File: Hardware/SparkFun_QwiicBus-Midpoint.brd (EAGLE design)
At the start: 45.7 x 27.9 mm, 69 parts, among them J1 QWIIC, J2 QWIIC, J3 RJ45, J7 RJ45, U1 PCA9615, U2 3.3V

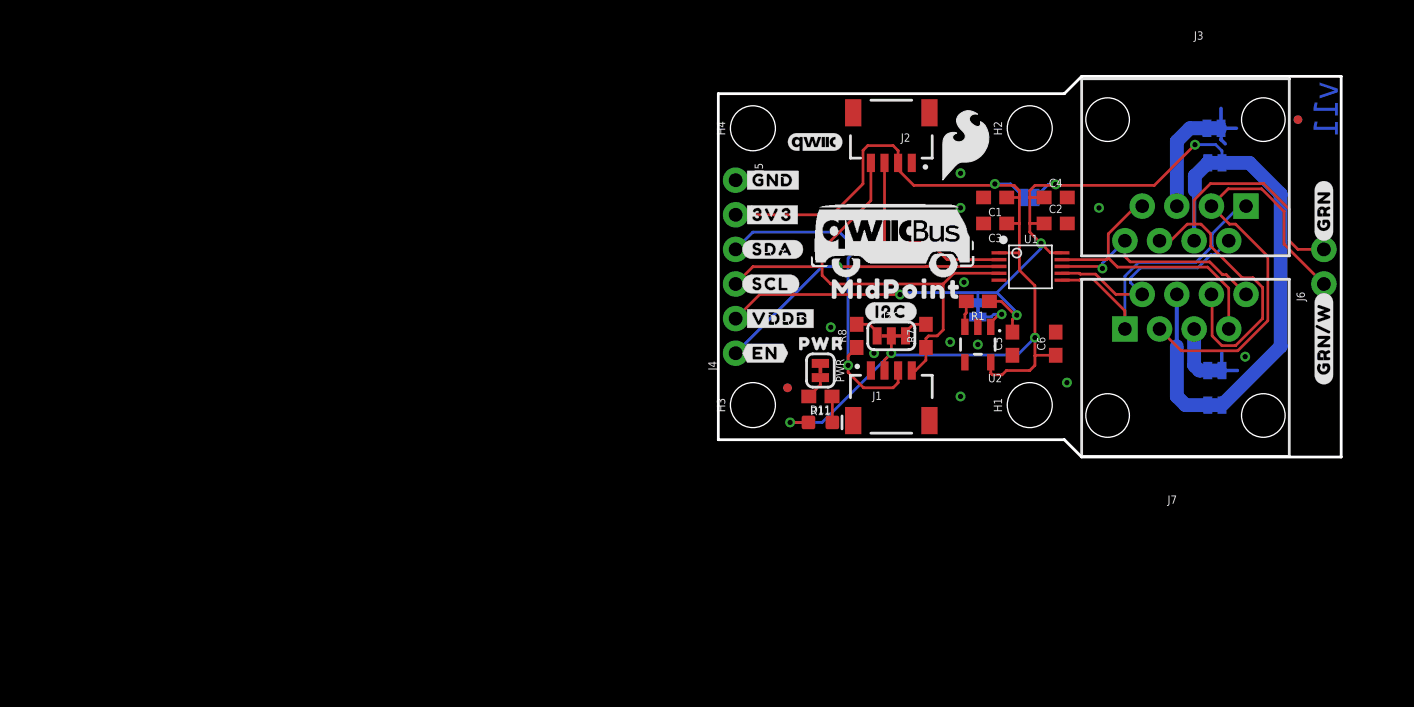
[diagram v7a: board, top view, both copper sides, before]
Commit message: adding buck regulator
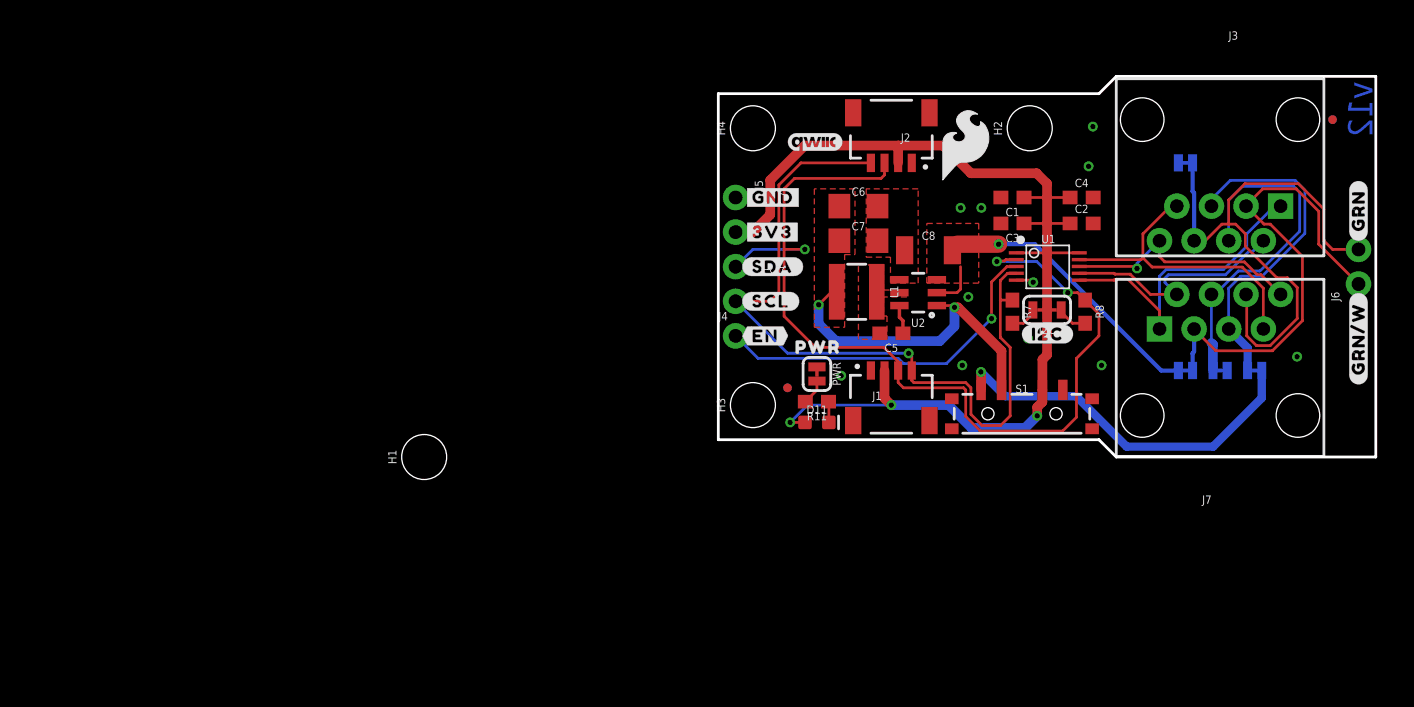
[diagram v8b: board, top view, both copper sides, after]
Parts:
- removed A-B: JUMPER-SMT_2_NO_SILK, SparkFun-Jumpers:SMT-JUMPER_2_NO_SILK
- removed JP5, JP6, VREG: JUMPER-SMT_2_NC_TRACE_SILK, SparkFun-Jumpers:SMT-JUMPER_2_NC_TRACE_SILK
- removed R1: 100k, SparkFun-Resistors:0603
- removed U$11: (no value), output:#A#B#0
- removed U$16, U$18, U$19, U$5: (no value), output:#VDDB#0
- removed U$17: (no value), output:#VREG#0
- removed U$20, U$21: (no value), output:#GND#0
- removed U$28: (no value), output:MIDPOINT0
- removed U$29: (no value), QwiicBus#working#Logo#jpg (2):QWIICBUS#WORKING#LOGO#JPG
- added C7: 22uF, SparkFun-Capacitors:1206
- added C8: 10uF, SparkFun-Capacitors:1210
- added HV, HVGND: JUMPER-SMT_2_NC_TRACE_SILK, SparkFun-Jumpers:SMT-JUMPER_2_NC_TRACE_SILK
- added L1: 4.7μH, SparkFun-Coils:INDUCTOR_4X4MM
- added S1: (no value), SparkFun-Switches:SWITCH_SP3T_SMD
- C5: value 1.0uF -> 0.1uF
- C6: value 1.0uF -> 22uF; device SparkFun-Capacitors:0603 -> SparkFun-Capacitors:1206
- J4: device SparkFun-Connectors:1X02_NO_SILK -> SparkFun-Connectors:1X01_NO_SILK
- U2: value 3.3V -> AP63203; device SparkFun-IC-Power:SOT23-5 -> SparkFun-IC-Power:SOT23-6
- moved H1 44.6 mm to (-21.6, 0.00)
- moved GND\ 17.8 mm to (36.8, 6.35)
- moved C6 17.7 mm to (10.3, 18.4), turned to 0 degrees
- moved R8 16.9 mm to (26.9, 10.7), turned to 270 degrees
- moved VDD_B 15.5 mm to (39.4, 6.35)
- moved U$13 11.6 mm to (22.3, 9.02)
- moved I2C 11.6 mm to (24.1, 10.8), turned to 180 degrees
- moved C5 8.92 mm to (12.7, 9.08), turned to 180 degrees
- moved R7 6.59 mm to (21.6, 10.7), turned to 270 degrees
- moved U2 5.81 mm to (14.7, 12.1), turned to 90 degrees
- moved FD2 2.54 mm to (45.1, 24.8)
- moved FD4 2.54 mm to (45.1, 24.8)
- moved J3 2.54 mm to (36.8, 24.8)
- moved J6 2.54 mm to (47.0, 12.7)
- moved J7 2.54 mm to (36.8, 3.05)
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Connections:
- removed net N$1: J3.4, VDD_B.2
- removed net N$2: GND\.2, J3.5
- removed net N$5: J7.4, JP5.2
- removed net N$6: J7.5, JP6.2
- removed net VDD_A: A-B.1, C1.1, C3.1, C6.1, D11.A, I2C.2, J1.2, J2.2, J5.2, U1.1, U2.5
- new net 3.3V: C1.1, C2.1, C3.1, C4.1, D11.A, I2C.2, J1.2, J2.2, J5.2, S1.3, U1.1, U1.10
- new net BLUE_N: GND\.2, J3.4, J7.4
- new net BLUE_P: J3.5, J7.5, VDD_B.2
- new net VREG_3V3: C6.1, C7.1, L1.P$2, S1.2, U2.1
- new net VREG_IN: C8.2, HV.2, U2.2, U2.3
- net GND: now also C7.2, C8.1, HVGND.1, U2.4; no longer C5.1, JP6.1, U2.2
- net GRN_N: now also HVGND.2
- net GRN_P: now also HV.1
- net N$7: now also C5.1, U2.6; no longer R1.2, U2.3
- net N$8: now also C5.2, L1.P$1, U2.5; no longer U2.1, VREG.2
- net VDD_B: now also S1.1; no longer A-B.2, C2.1, C4.1, C5.2, J4.2, JP5.1, R1.1, U1.10, VREG.1
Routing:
- net 3.3V: track 0.00 -> 81.7 mm, vias 0 -> 3
- net VDD_A: track 76.6 -> 0.00 mm, vias 4 -> 0
- net VDD_B: track 81.0 -> 27.7 mm, vias 5 -> 1
- net SDA: track 43.0 -> 71.4 mm, vias 2 -> 3
- net BLUE_N: track 0.00 -> 25.7 mm
- net BLUE_P: track 0.00 -> 25.3 mm
- net VREG_3V3: track 0.00 -> 24.4 mm, vias 0 -> 2
- net VREG_IN: track 0.00 -> 23.8 mm, vias 0 -> 1
- net SCL: track 38.0 -> 57.7 mm, vias 0 -> 1
- net N$5: track 10.9 -> 0.00 mm
- net N$2: track 8.33 -> 0.00 mm
- net N$1: track 7.03 -> 0.00 mm
- net GRN_N: track 35.9 -> 41.6 mm
- net GND: track 6.33 -> 1.31 mm, vias 12 -> 11
- net N$6: track 4.73 -> 0.00 mm
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- added copper zone on layer 1, net N$8
- added copper zone on layer 1, net VREG_3V3
- added copper zone on layer 1, net VREG_IN
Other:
- board size 45.7 x 27.9 mm -> 48.3 x 27.9 mm
- board text added: "v12"
- board text removed: "v11"
